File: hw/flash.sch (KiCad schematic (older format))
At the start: 4 parts, among them U4 AT25xxx

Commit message: epd-clock: hw v0.2
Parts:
- renumbered R9 to R8, R10 to R9
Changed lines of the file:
@@
 $EndComp
 $Comp
-L power:GND #PWR040
+L power:GND #PWR043
 U 1 1 6122BC9D
 P 6000 3700
-F 0 "#PWR040" H 6000 3450 50  0001 C CNN
+F 0 "#PWR043" H 6000 3450 50  0001 C CNN
 F 1 "GND" H 6005 3527 50  0000 C CNN
 F 2 "" H 6000 3700 50  0001 C CNN
@@
 $EndComp
 $Comp
-L power:+3V3 #PWR039
+L power:+3V3 #PWR042
 U 1 1 6122C087
 P 6000 3000
-F 0 "#PWR039" H 6000 2850 50  0001 C CNN
+F 0 "#PWR042" H 6000 2850 50  0001 C CNN
 F 1 "+3V3" H 6015 3173 50  0000 C CNN
 F 2 "" H 6000 3000 50  0001 C CNN
@@
 $EndComp
 $Comp
-L power:+3V3 #PWR041
+L power:+3V3 #PWR044
 U 1 1 6123B32A
 P 7000 3250
-F 0 "#PWR041" H 7000 3100 50  0001 C CNN
+F 0 "#PWR044" H 7000 3100 50  0001 C CNN
 F 1 "+3V3" H 7015 3423 50  0000 C CNN
 F 2 "" H 7000 3250 50  0001 C CNN
@@
 $EndComp
 $Comp
-L power:GND #PWR042
+L power:GND #PWR045
 U 1 1 6123B7F6
 P 7000 3650
-F 0 "#PWR042" H 7000 3400 50  0001 C CNN
+F 0 "#PWR045" H 7000 3400 50  0001 C CNN
 F 1 "GND" H 7005 3477 50  0000 C CNN
 F 2 "" H 7000 3650 50  0001 C CNN
@@
 	7000 3650 7000 3550
 $Comp
-L Device:R R9
+L Device:R R8
 U 1 1 610BAE93
 P 5150 3300
-F 0 "R9" V 5050 3200 50  0000 C CNN
+F 0 "R8" V 5050 3200 50  0000 C CNN
 F 1 "10K" V 5050 3400 50  0000 C CNN
 F 2 "Resistor_SMD:R_0603_1608Metric" V 5080 3300 50  0001 C CNN
@@
 $EndComp
 $Comp
-L Device:R R10
+L Device:R R9
 U 1 1 610BB93F
 P 5150 3400
-F 0 "R10" V 5250 3300 50  0000 C CNN
+F 0 "R9" V 5250 3300 50  0000 C CNN
 F 1 "10K" V 5250 3500 50  0000 C CNN
 F 2 "Resistor_SMD:R_0603_1608Metric" V 5080 3400 50  0001 C CNN

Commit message: epd-clock: hw: v0.2
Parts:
- renumbered C19 to C18, R8 to R13, R9 to R14, U4 to U3
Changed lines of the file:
@@
 $EndDescr
 $Comp
-L Memory_EEPROM:AT25xxx U4
+L Memory_EEPROM:AT25xxx U3
 U 1 1 6122B52B
 P 6000 3400
-F 0 "U4" H 5800 3700 50  0000 C CNN
+F 0 "U3" H 5800 3700 50  0000 C CNN
 F 1 "AT25xxx" H 6200 3650 50  0000 C CNN
 F 2 "Package_SO:SOIC-8_5.275x5.275mm_P1.27mm" H 6000 3400 50  0001 C CNN
@@
 $EndComp
 $Comp
-L power:GND #PWR043
+L power:GND #PWR041
 U 1 1 6122BC9D
 P 6000 3700
-F 0 "#PWR043" H 6000 3450 50  0001 C CNN
+F 0 "#PWR041" H 6000 3450 50  0001 C CNN
 F 1 "GND" H 6005 3527 50  0000 C CNN
 F 2 "" H 6000 3700 50  0001 C CNN
@@
 $EndComp
 $Comp
-L power:+3V3 #PWR042
+L power:+3V3 #PWR040
 U 1 1 6122C087
 P 6000 3000
-F 0 "#PWR042" H 6000 2850 50  0001 C CNN
+F 0 "#PWR040" H 6000 2850 50  0001 C CNN
 F 1 "+3V3" H 6015 3173 50  0000 C CNN
 F 2 "" H 6000 3000 50  0001 C CNN
@@
 CS
 $Comp
-L Device:C C19
+L Device:C C18
 U 1 1 6123AFE1
 P 7000 3400
-F 0 "C19" H 7115 3446 50  0000 L CNN
+F 0 "C18" H 7115 3446 50  0000 L CNN
 F 1 "0.1uF" H 7115 3355 50  0000 L CNN
 F 2 "Capacitor_SMD:C_0603_1608Metric" H 7038 3250 50  0001 C CNN
@@
 $EndComp
 $Comp
-L power:+3V3 #PWR044
+L power:+3V3 #PWR042
 U 1 1 6123B32A
 P 7000 3250
-F 0 "#PWR044" H 7000 3100 50  0001 C CNN
+F 0 "#PWR042" H 7000 3100 50  0001 C CNN
 F 1 "+3V3" H 7015 3423 50  0000 C CNN
 F 2 "" H 7000 3250 50  0001 C CNN
@@
 $EndComp
 $Comp
-L power:GND #PWR045
+L power:GND #PWR043
 U 1 1 6123B7F6
 P 7000 3650
-F 0 "#PWR045" H 7000 3400 50  0001 C CNN
+F 0 "#PWR043" H 7000 3400 50  0001 C CNN
 F 1 "GND" H 7005 3477 50  0000 C CNN
 F 2 "" H 7000 3650 50  0001 C CNN
@@
 	7000 3650 7000 3550
 $Comp
-L Device:R R8
+L Device:R R13
 U 1 1 610BAE93
 P 5150 3300
-F 0 "R8" V 5050 3200 50  0000 C CNN
+F 0 "R13" V 5050 3200 50  0000 C CNN
 F 1 "10K" V 5050 3400 50  0000 C CNN
 F 2 "Resistor_SMD:R_0603_1608Metric" V 5080 3300 50  0001 C CNN
@@
 $EndComp
 $Comp
-L Device:R R9
+L Device:R R14
 U 1 1 610BB93F
 P 5150 3400
-F 0 "R9" V 5250 3300 50  0000 C CNN
+F 0 "R14" V 5250 3300 50  0000 C CNN
 F 1 "10K" V 5250 3500 50  0000 C CNN
 F 2 "Resistor_SMD:R_0603_1608Metric" V 5080 3400 50  0001 C CNN

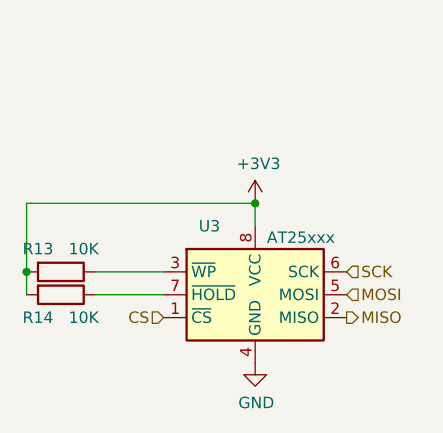
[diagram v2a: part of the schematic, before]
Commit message: hw: 合并电源网络
取消墨水屏电源控制mos与独立电源域，墨水屏使用深度休眠模式，共用主
电源域。
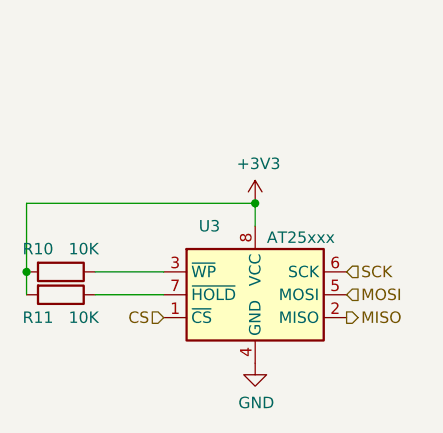
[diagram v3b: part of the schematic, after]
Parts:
- renumbered R13 to R10, R14 to R11
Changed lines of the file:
@@
 $EndComp
 $Comp
-L power:GND #PWR041
+L power:GND #PWR039
 U 1 1 6122BC9D
 P 6000 3700
-F 0 "#PWR041" H 6000 3450 50  0001 C CNN
+F 0 "#PWR039" H 6000 3450 50  0001 C CNN
 F 1 "GND" H 6005 3527 50  0000 C CNN
 F 2 "" H 6000 3700 50  0001 C CNN
@@
 $EndComp
 $Comp
-L power:+3V3 #PWR040
+L power:+3V3 #PWR038
 U 1 1 6122C087
 P 6000 3000
-F 0 "#PWR040" H 6000 2850 50  0001 C CNN
+F 0 "#PWR038" H 6000 2850 50  0001 C CNN
 F 1 "+3V3" H 6015 3173 50  0000 C CNN
 F 2 "" H 6000 3000 50  0001 C CNN
@@
 $EndComp
 $Comp
-L power:+3V3 #PWR042
+L power:+3V3 #PWR040
 U 1 1 6123B32A
 P 7000 3250
-F 0 "#PWR042" H 7000 3100 50  0001 C CNN
+F 0 "#PWR040" H 7000 3100 50  0001 C CNN
 F 1 "+3V3" H 7015 3423 50  0000 C CNN
 F 2 "" H 7000 3250 50  0001 C CNN
@@
 $EndComp
 $Comp
-L power:GND #PWR043
+L power:GND #PWR041
 U 1 1 6123B7F6
 P 7000 3650
-F 0 "#PWR043" H 7000 3400 50  0001 C CNN
+F 0 "#PWR041" H 7000 3400 50  0001 C CNN
 F 1 "GND" H 7005 3477 50  0000 C CNN
 F 2 "" H 7000 3650 50  0001 C CNN
@@
 	7000 3650 7000 3550
 $Comp
-L Device:R R13
+L Device:R R10
 U 1 1 610BAE93
 P 5150 3300
-F 0 "R13" V 5050 3200 50  0000 C CNN
+F 0 "R10" V 5050 3200 50  0000 C CNN
 F 1 "10K" V 5050 3400 50  0000 C CNN
 F 2 "Resistor_SMD:R_0603_1608Metric" V 5080 3300 50  0001 C CNN
@@
 $EndComp
 $Comp
-L Device:R R14
+L Device:R R11
 U 1 1 610BB93F
 P 5150 3400
-F 0 "R14" V 5250 3300 50  0000 C CNN
+F 0 "R11" V 5250 3300 50  0000 C CNN
 F 1 "10K" V 5250 3500 50  0000 C CNN
 F 2 "Resistor_SMD:R_0603_1608Metric" V 5080 3400 50  0001 C CNN
